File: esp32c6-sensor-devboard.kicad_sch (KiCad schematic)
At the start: 78 parts, among them J1 Conn_01x04_Pin, J2 Micro_SD_Card_Det1, J3 Screw_Terminal_01x02, J4 USB_C_Receptacle_USB2.0_14P, J5 Screw_Terminal_01x02, J6 Screw_Terminal_01x06, J7 Screw_Terminal_01x04, SW1 SW_Push, SW2 SW_Push, U1 ESP32-C6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

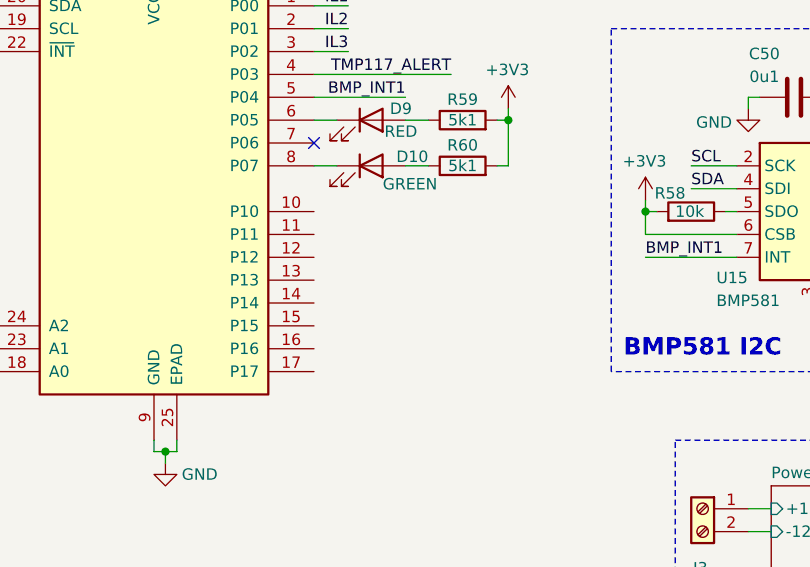
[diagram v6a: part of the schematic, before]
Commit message: schem: add dip switches
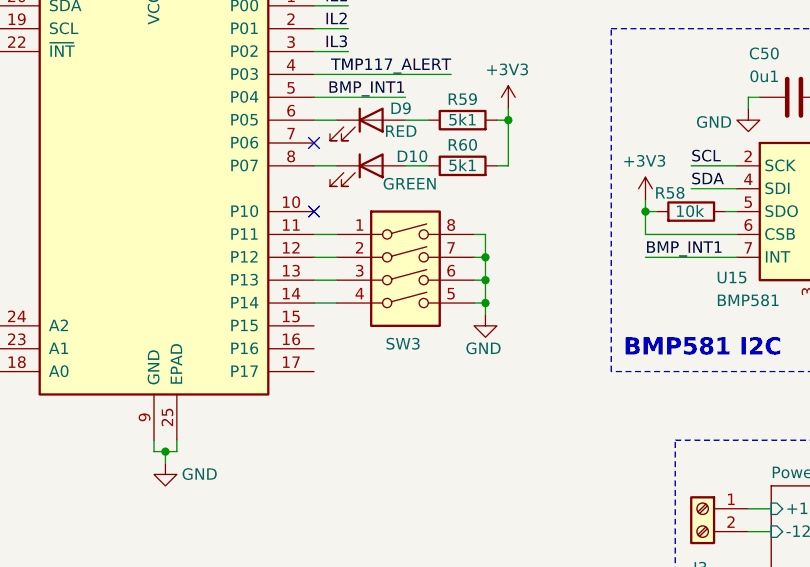
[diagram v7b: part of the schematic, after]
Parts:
- added SW3: SW_DIP_x04, Button_Switch_THT:SW_DIP_SPSTx04_Slide_9.78x12.34mm_W7.62mm_P2.54mm, symbol Switch:SW_DIP_x04
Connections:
- net GND: now also SW3.5, SW3.6, SW3.7, SW3.8
- net at U11.11 (P11): now also SW3.1
- net at U11.12 (P12): now also SW3.2
- net at U11.13 (P13): now also SW3.3
- net at U11.14 (P14): now also SW3.4
- no-connect marks 2 -> 3

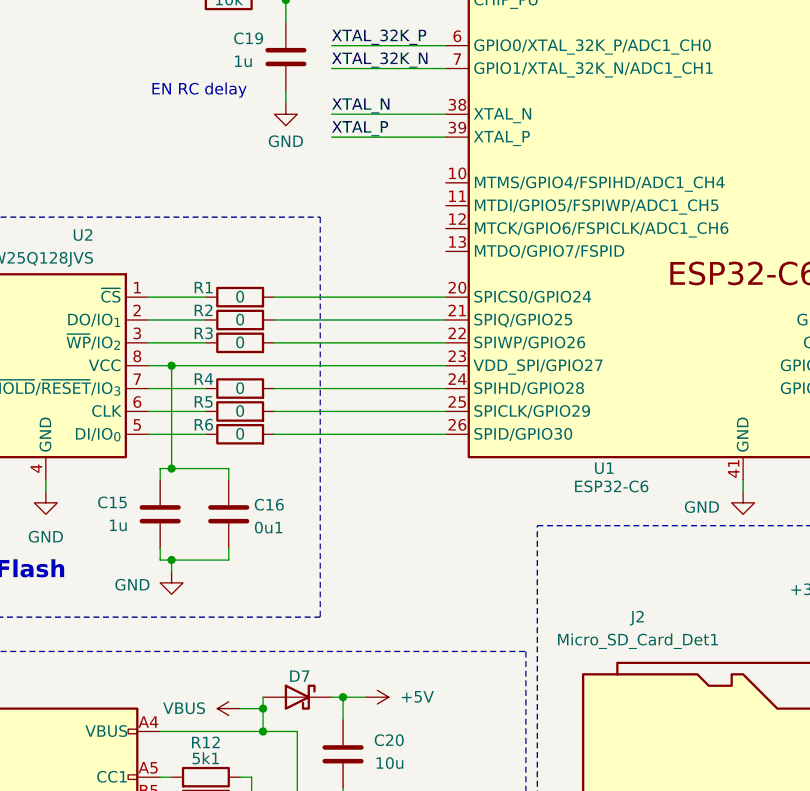
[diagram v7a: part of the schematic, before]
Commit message: schem: add spare pins headers
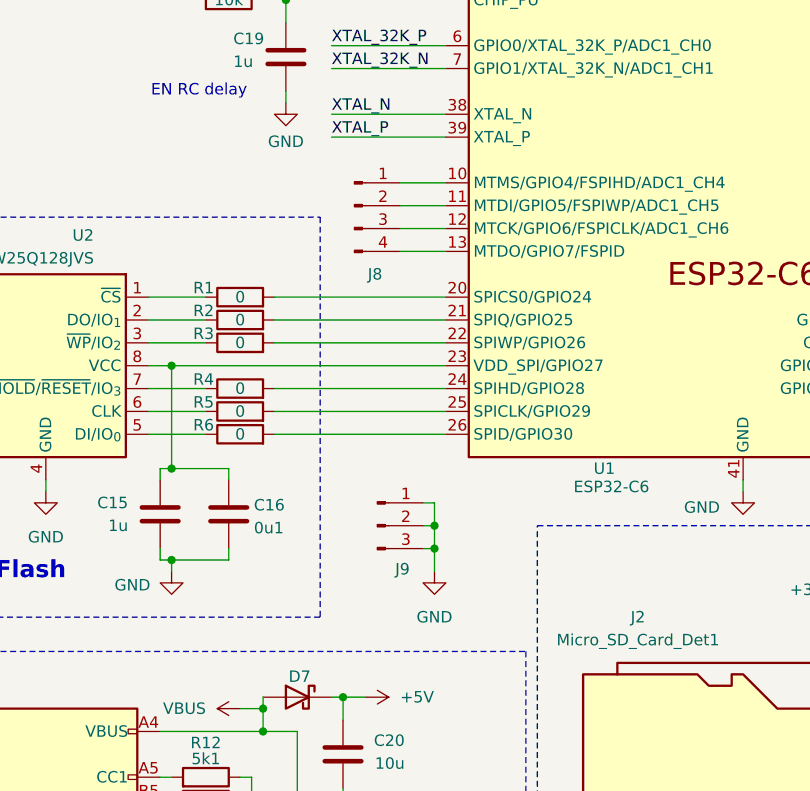
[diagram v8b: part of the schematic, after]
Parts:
- added J8: Conn_01x04_Pin, symbol Connector:Conn_01x04_Pin
- added J9: Conn_01x03_Pin, symbol Connector:Conn_01x03_Pin
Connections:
- net GND: now also J9.1 (Pin_1), J9.2 (Pin_2), J9.3 (Pin_3)
- net at U1.10 (MTMS/GPIO4/FSPIHD/ADC1_CH4): now also J8.1 (Pin_1)
- net at U1.11 (MTDI/GPIO5/FSPIWP/ADC1_CH5): now also J8.2 (Pin_2)
- net at U1.12 (MTCK/GPIO6/FSPICLK/ADC1_CH6): now also J8.3 (Pin_3)
- net at U1.13 (MTDO/GPIO7/FSPID): now also J8.4 (Pin_4)
